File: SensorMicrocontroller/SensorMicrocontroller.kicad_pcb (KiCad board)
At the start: 2 copper layers, 100 x 100 mm, 41 parts, among them J1 JST B4B-PH-SM4-TB, J2 JST B4B-PH-SM4-TB, J3 JST B6B-PH-SM4-TB, J4 JST B4B-PH-SM4-TB, J5 JST B4B-PH-SM4-TB, J8 12V Connector, J9 Light Connector, Q1 DMT6009LCT, Q2 DMT6009LCT, U1 ADS1115IDGS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

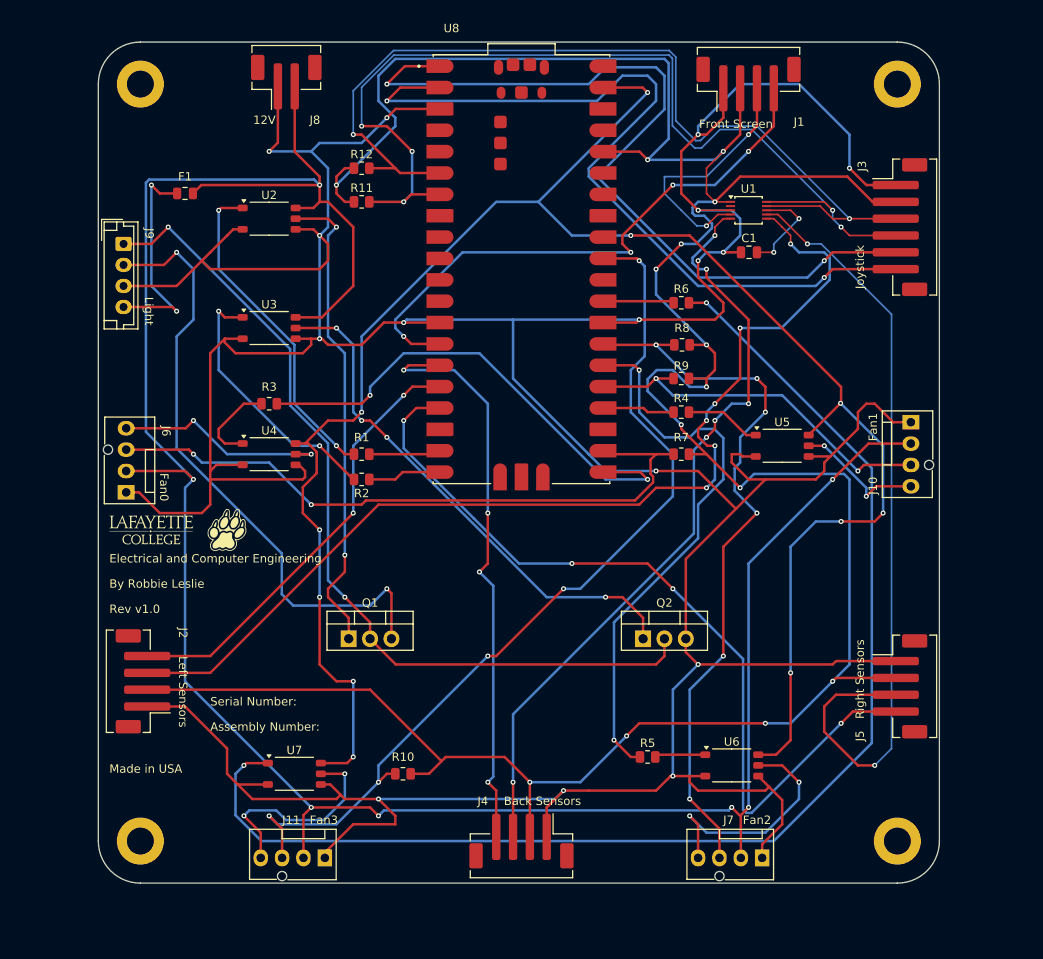
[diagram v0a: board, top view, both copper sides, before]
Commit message: Updated trace width for high current components
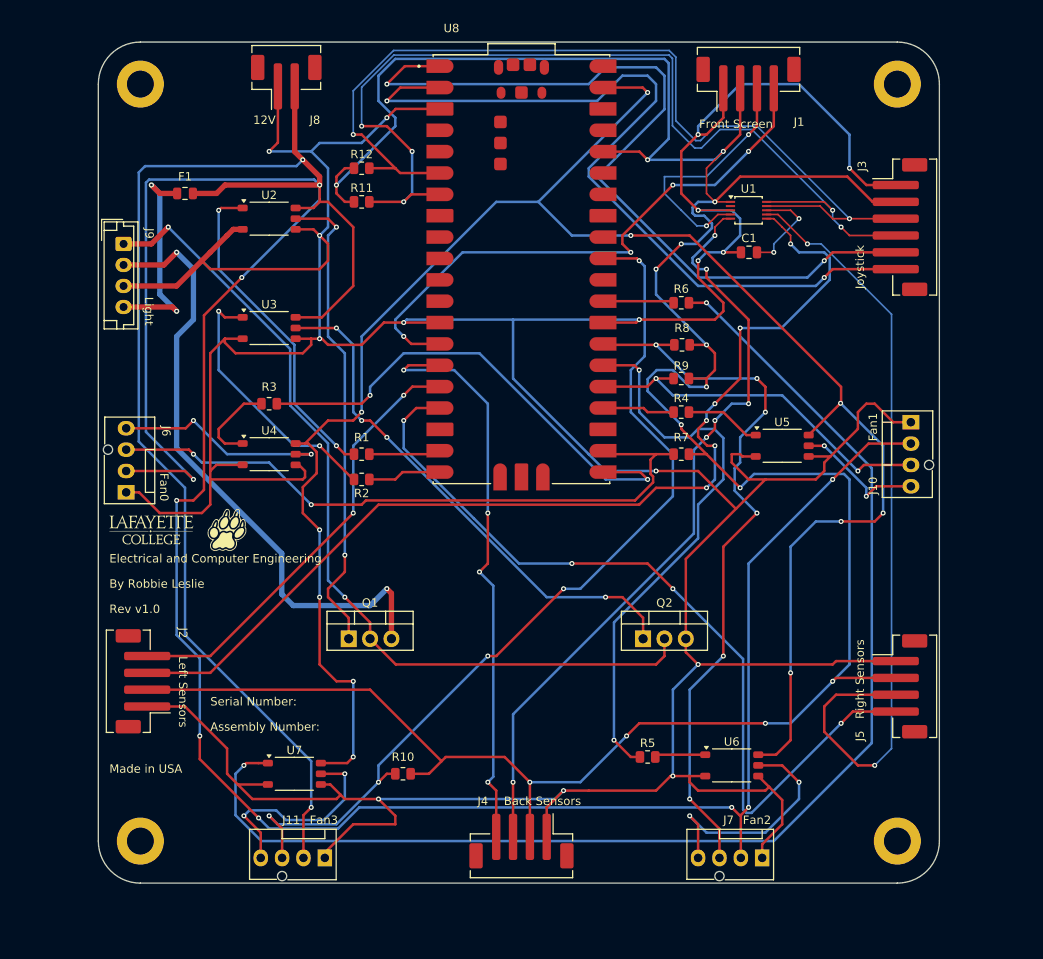
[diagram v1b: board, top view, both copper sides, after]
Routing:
- net /12V: track 286.2 -> 439.2 mm, vias 7 -> 11
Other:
- board text added: "1/31/25"
- board text removed: "1/28/25"

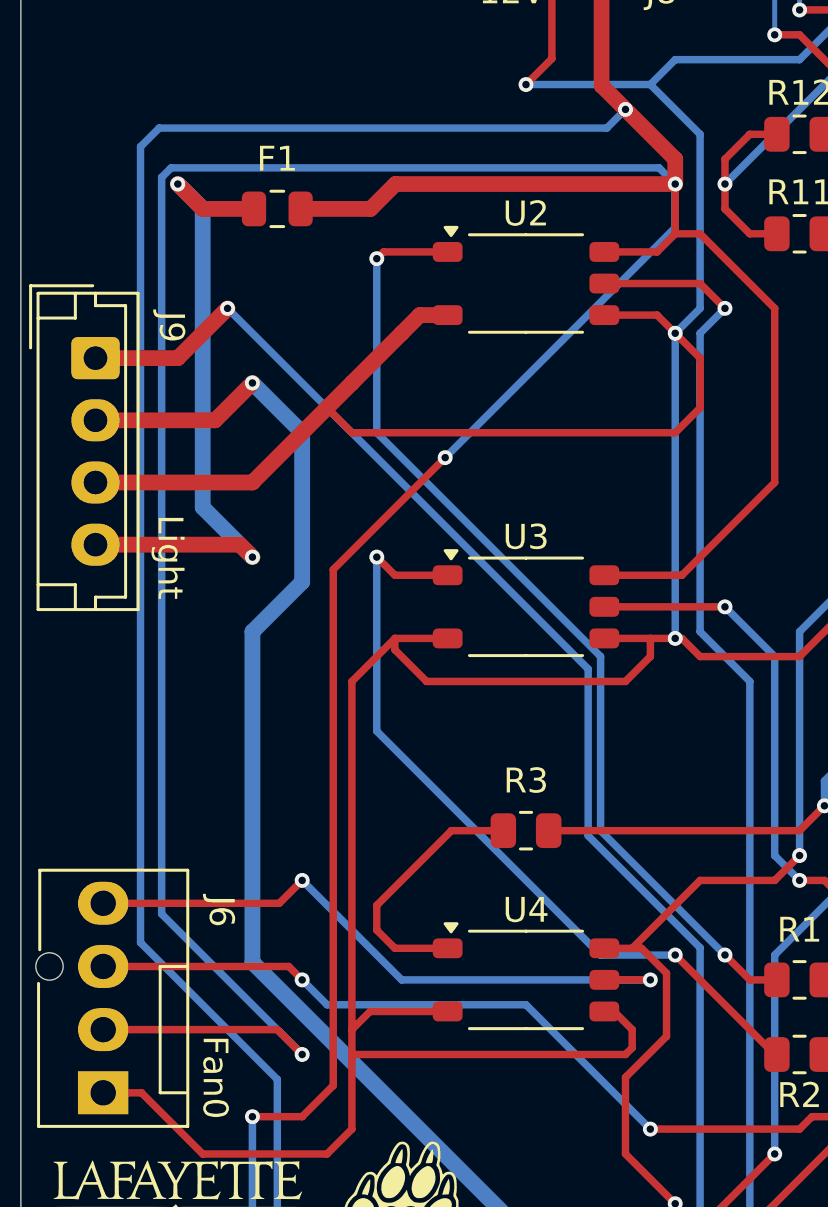
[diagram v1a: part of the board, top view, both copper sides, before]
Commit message: Fixed trace error
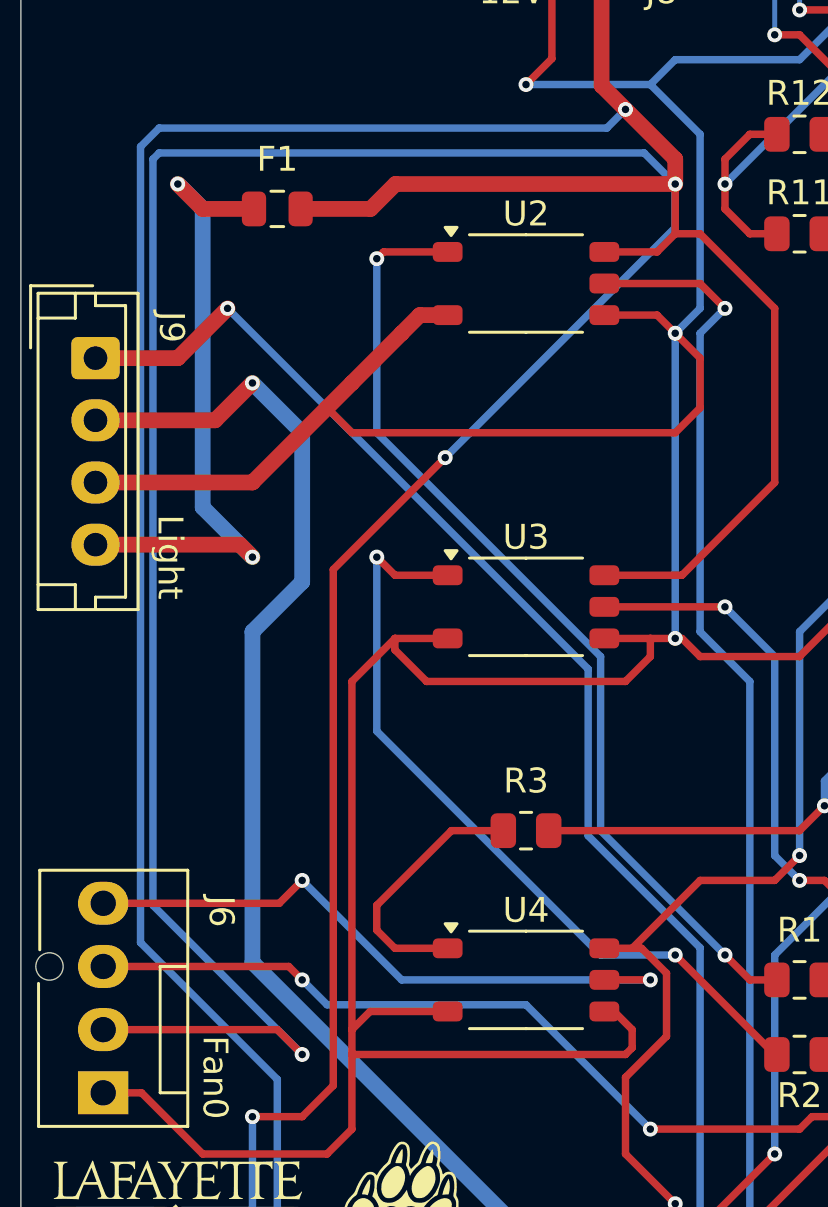
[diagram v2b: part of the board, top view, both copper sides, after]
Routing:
- net /12V: track 439.2 -> 440.6 mm
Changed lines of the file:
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@@
-	)
-	(segment
-		(start 100.730761 64.35)
-		(end 120.35 64.35)
-		(width 0.3)
-		(layer "B.Cu")
-		(net 17)
-	)
-	(segment
-		(start 100.35 94.35)
-		(end 100.35 64.730761)
-		(width 0.3)
-		(layer "B.Cu")
-		(net 17)
 	)
 	(segment
@@
 	)
 	(segment
+		(start 119.75 63.75)
+		(end 121 65)
+		(width 0.3)
+		(layer "B.Cu")
+		(net 17)
+	)
+	(segment
 		(start 106.75 130.5)
 		(end 106.75 121.25)
+		(width 0.3)
+		(layer "B.Cu")
+		(net 17)
+	)
+	(segment
+		(start 100 94)
+		(end 100 64)
+		(width 0.3)
+		(layer "B.Cu")
+		(net 17)
+	)
+	(segment
+		(start 100 64)
+		(end 100.25 63.75)
 		(width 0.3)
 		(layer "B.Cu")
@@
 	)
 	(segment
-		(start 100.35 64.730761)
-		(end 100.730761 64.35)
+		(start 106 100)
+		(end 100 94)
 		(width 0.3)
 		(layer "B.Cu")
@@
 		(start 182 100)
 		(end 172 110)
-		(width 0.3)
-		(layer "B.Cu")
-		(net 17)
-	)
-	(segment
-		(start 106 100)
-		(end 100.35 94.35)
 		(width 0.3)
 		(layer "B.Cu")
@@
 	)
 	(segment
-		(start 120.35 64.35)
-		(end 121 65)
-		(width 0.3)
-		(layer "B.Cu")
-		(net 17)
-	)
-	(segment
 		(start 105 101)
 		(end 105 118.5)
@@
 		(width 0.3)
 		(layer "B.Cu")
+		(net 17)
+	)
+	(segment
+		(start 100.25 63.75)
+		(end 119.75 63.75)
+		(width 0.3)
+		(layer "B.Cu")

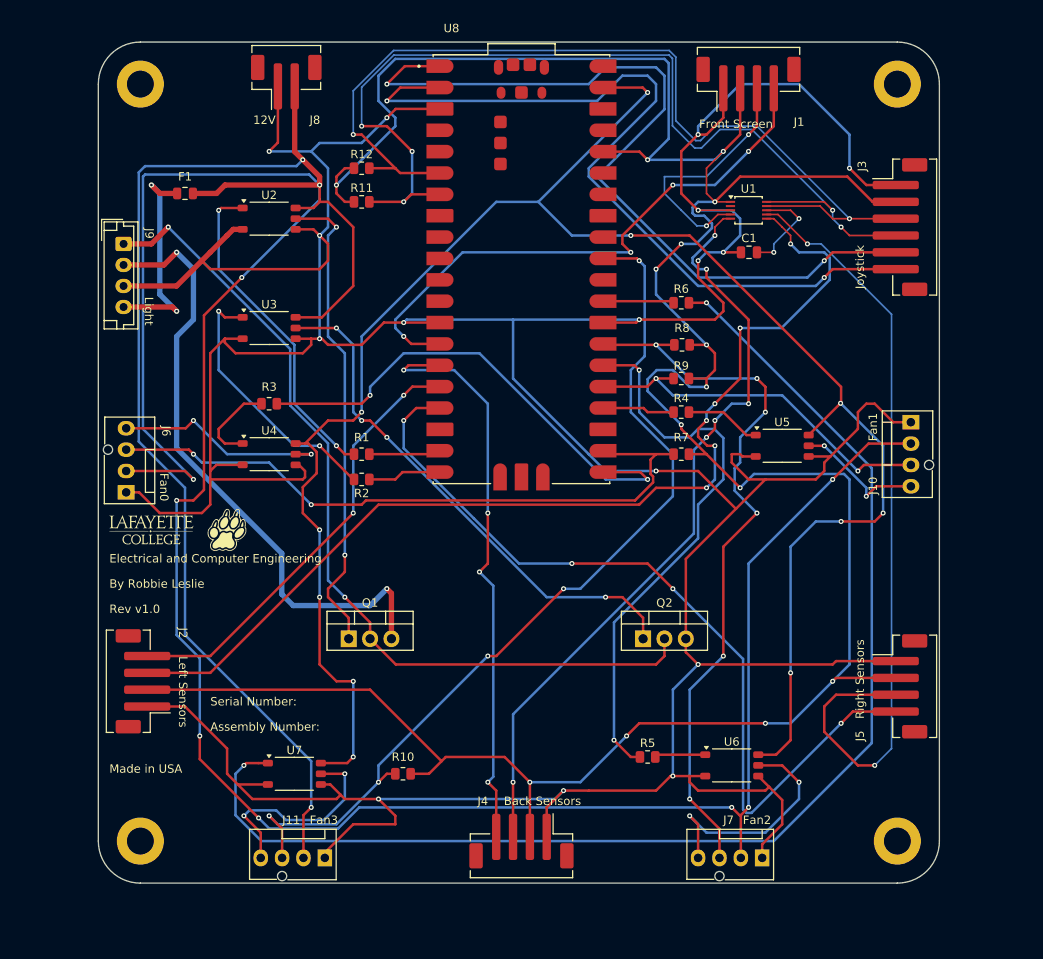
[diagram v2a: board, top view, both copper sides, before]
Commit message: Updated GND trace widths for more current
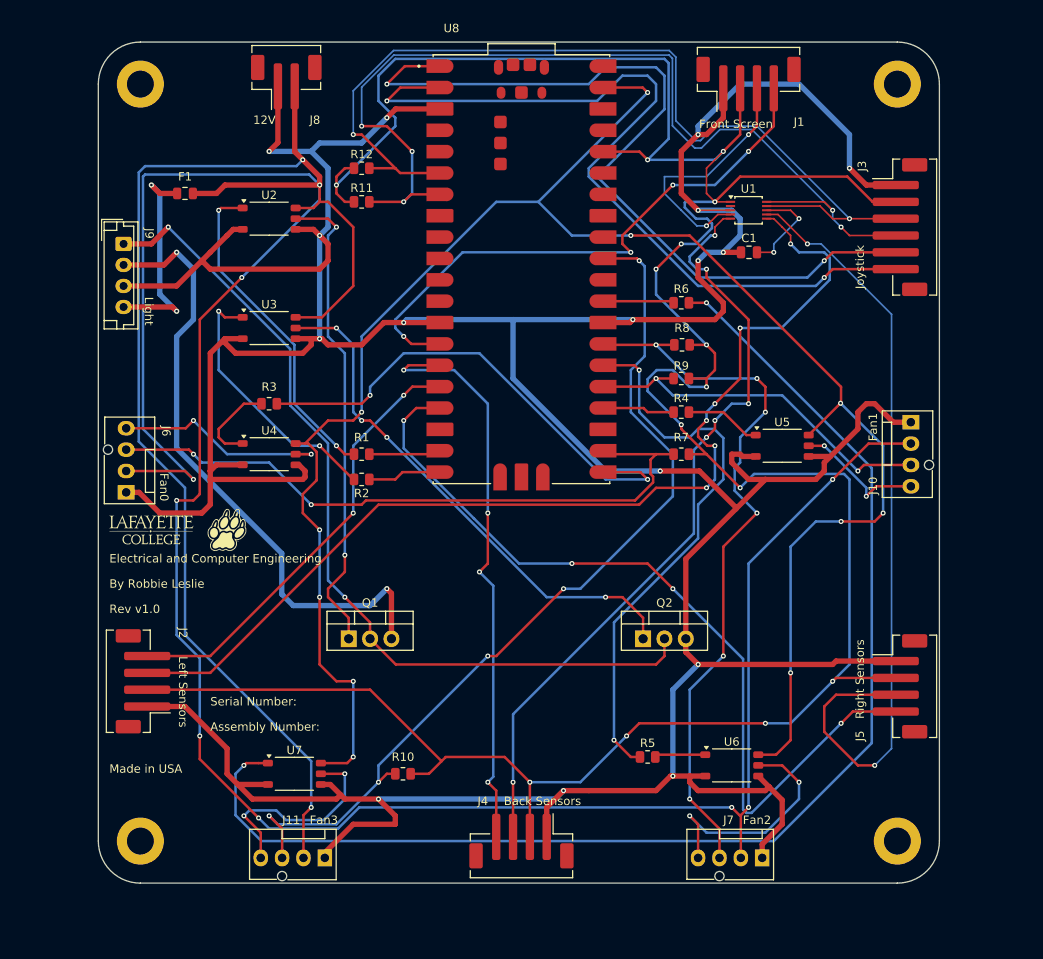
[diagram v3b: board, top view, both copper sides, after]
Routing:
- net /3.3V: track 341.9 -> 343.7 mm
- net /US1: track 91.9 -> 92.6 mm
- net /GND: track 561.4 -> 560.7 mm

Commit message: Swapped M3 screws to ISO 7380
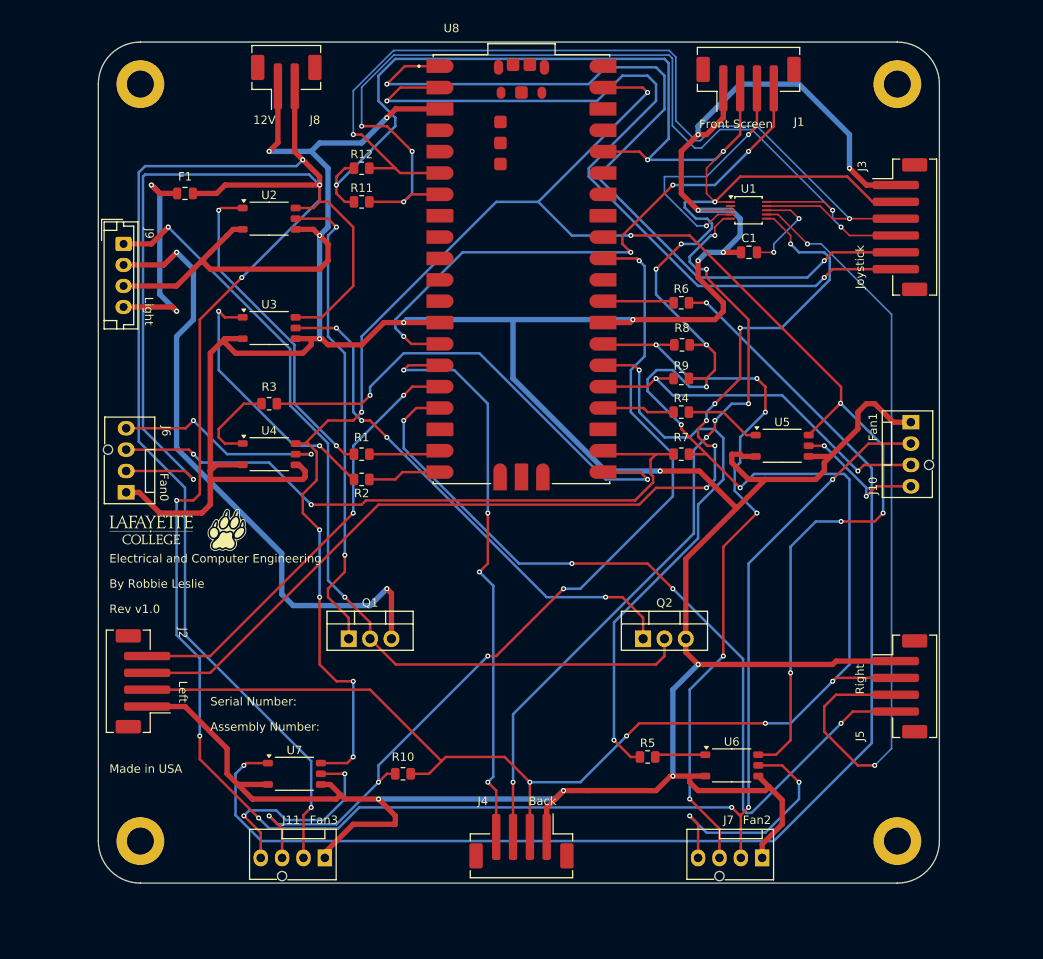
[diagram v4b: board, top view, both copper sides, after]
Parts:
- H1, H2, H3, H4: footprint MountingHole:MountingHole_3.2mm_M3_DIN965_Pad -> MountingHole:MountingHole_3.2mm_M3_ISO7380_Pad
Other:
- board text added: "2/1/25"
- board text removed: "1/31/25"
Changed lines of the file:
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@@
 		)
 	)
-	(footprint "MountingHole:MountingHole_3.2mm_M3_DIN965_Pad"
+	(footprint "MountingHole:MountingHole_3.2mm_M3_ISO7380_Pad"
 		(layer "F.Cu")
 		(at 99.69 53)
-		(descr "Mounting Hole 3.2mm, M3, DIN965")
-		(tags "mounting hole 3.2mm m3 din965")
+		(descr "Mounting Hole 3.2mm, M3, ISO7380")
+		(tags "mounting hole 3.2mm m3 iso7380")
 		(property "Reference" "H1"
-			(at 0 -3.8 0)
+			(at 0 -3.85 0)
 			(layer "F.SilkS")
 			(hide yes)
@@
 		)
 		(property "Value" "MountingHole"
-			(at 0 3.8 0)
+			(at 0 3.85 0)
 			(layer "F.Fab")
 			(effects
@@
 			)
 		)
-		(property "Footprint" "MountingHole:MountingHole_3.2mm_M3_DIN965_Pad"
+		(property "Footprint" "MountingHole:MountingHole_3.2mm_M3_ISO7380_Pad"
 			(at 0 0 0)
 			(unlocked yes)
@@
 		(fp_circle
 			(center 0 0)
-			(end 2.8 0)
+			(end 2.85 0)
 			(stroke
 				(width 0.15)
@@
 		(fp_circle
 			(center 0 0)
-			(end 3.05 0)
+			(end 3.1 0)
 			(stroke
 				(width 0.05)
@@
 		(pad "1" thru_hole circle
 			(at 0 0)
-			(size 5.6 5.6)
+			(size 5.7 5.7)
 			(drill 3.2)
 			(layers "*.Cu" "*.Mask")
@@
 			)
 		)
-		(property "Header Connection" "Right Sensors"
+		(property "Header Connection" "Right"
 			(at -0.85 4.75 90)
 			(unlocked yes)
@@
 			)
 		)
-		(property "Header Connection" "Left Sensors"
+		(property "Header Connection" "Left"
 			(at -1.25 4.75 -90)
 			(unlocked yes)
@@
 		)
 	)
-	(footprint "MountingHole:MountingHole_3.2mm_M3_DIN965_Pad"
+	(footprint "MountingHole:MountingHole_3.2mm_M3_ISO7380_Pad"
 		(layer "F.Cu")
 		(at 189.69 53)
-		(descr "Mounting Hole 3.2mm, M3, DIN965")
-		(tags "mounting hole 3.2mm m3 din965")
+		(descr "Mounting Hole 3.2mm, M3, ISO7380")
+		(tags "mounting hole 3.2mm m3 iso7380")
 		(property "Reference" "H2"
-			(at 0 -3.8 0)
+			(at 0 -3.85 0)
 			(layer "F.SilkS")
 			(hide yes)
@@
 		)
 		(property "Value" "MountingHole"
-			(at 0 3.8 0)
+			(at 0 3.85 0)
 			(layer "F.Fab")
 			(effects
@@
 			)
 		)
-		(property "Footprint" "MountingHole:MountingHole_3.2mm_M3_DIN965_Pad"
+		(property "Footprint" "MountingHole:MountingHole_3.2mm_M3_ISO7380_Pad"
 			(at 0 0 0)
 			(unlocked yes)
@@
 		(fp_circle
 			(center 0 0)
-			(end 2.8 0)
+			(end 2.85 0)
 			(stroke
 				(width 0.15)
@@
 		(fp_circle
 			(center 0 0)
-			(end 3.05 0)
+			(end 3.1 0)
 			(stroke
 				(width 0.05)
@@
 		(pad "1" thru_hole circle
 			(at 0 0)
-			(size 5.6 5.6)
+			(size 5.7 5.7)
 			(drill 3.2)
 			(layers "*.Cu" "*.Mask")
@@
 			)
 		)
-		(property "Header Connection" "Back Sensors"
+		(property "Header Connection" "Back"
 			(at -2.5 4.75 0)
 			(unlocked yes)
@@
 		)
 	)
-	(footprint "MountingHole:MountingHole_3.2mm_M3_DIN965_Pad"
+	(footprint "MountingHole:MountingHole_3.2mm_M3_ISO7380_Pad"
 		(layer "F.Cu")
 		(at 99.69 143)
-		(descr "Mounting Hole 3.2mm, M3, DIN965")
-		(tags "mounting hole 3.2mm m3 din965")
+		(descr "Mounting Hole 3.2mm, M3, ISO7380")
+		(tags "mounting hole 3.2mm m3 iso7380")
 		(property "Reference" "H3"
-			(at 0 -3.8 0)
+			(at 0 -3.85 0)
 			(layer "F.SilkS")
 			(hide yes)
@@
 		)
 		(property "Value" "MountingHole"
-			(at 0 3.8 0)
+			(at 0 3.85 0)
 			(layer "F.Fab")
 			(effects
@@
 			)
 		)
-		(property "Footprint" "MountingHole:MountingHole_3.2mm_M3_DIN965_Pad"
+		(property "Footprint" "MountingHole:MountingHole_3.2mm_M3_ISO7380_Pad"
 			(at 0 0 0)
 			(unlocked yes)
@@
 		(fp_circle
 			(center 0 0)
-			(end 2.8 0)
+			(end 2.85 0)
 			(stroke
 				(width 0.15)
@@
 		(fp_circle
 			(center 0 0)
-			(end 3.05 0)
+			(end 3.1 0)
 			(stroke
 				(width 0.05)
@@
 		(pad "1" thru_hole circle
 			(at 0 0)
-			(size 5.6 5.6)
+			(size 5.7 5.7)
 			(drill 3.2)
 			(layers "*.Cu" "*.Mask")
@@
 		)
 	)
-	(footprint "MountingHole:MountingHole_3.2mm_M3_DIN965_Pad"
+	(footprint "MountingHole:MountingHole_3.2mm_M3_ISO7380_Pad"
 		(layer "F.Cu")
 		(at 189.69 143)
-		(descr "Mounting Hole 3.2mm, M3, DIN965")
-		(tags "mounting hole 3.2mm m3 din965")
+		(descr "Mounting Hole 3.2mm, M3, ISO7380")
+		(tags "mounting hole 3.2mm m3 iso7380")
 		(property "Reference" "H4"
-			(at 0 -3.8 0)
+			(at 0 -3.85 0)
 			(layer "F.SilkS")
 			(hide yes)
@@
 		)
 		(property "Value" "MountingHole"
-			(at 0 3.8 0)
+			(at 0 3.85 0)
 			(layer "F.Fab")
 			(effects
@@
 			)
 		)
-		(property "Footprint" "MountingHole:MountingHole_3.2mm_M3_DIN965_Pad"
+		(property "Footprint" "MountingHole:MountingHole_3.2mm_M3_ISO7380_Pad"
 			(at 0 0 0)
 			(unlocked yes)
@@
 		(fp_circle
 			(center 0 0)
-			(end 2.8 0)
+			(end 2.85 0)
 			(stroke
 				(width 0.15)
@@
 		(fp_circle
 			(center 0 0)
-			(end 3.05 0)
+			(end 3.1 0)
 			(stroke
 				(width 0.05)
@@
 		(pad "1" thru_hole circle
 			(at 0 0)
-			(size 5.6 5.6)
+			(size 5.7 5.7)
 			(drill 3.2)
 			(layers "*.Cu" "*.Mask")
@@
 		)
 	)
-	(gr_text "1/31/25"
+	(gr_text "2/1/25"
 		(at 206 194 0)
 		(layer "Cmts.User")
